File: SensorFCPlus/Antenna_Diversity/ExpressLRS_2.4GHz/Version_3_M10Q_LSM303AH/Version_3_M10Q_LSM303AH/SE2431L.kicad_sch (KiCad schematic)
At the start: 8 parts, among them U7 SE2431L-R

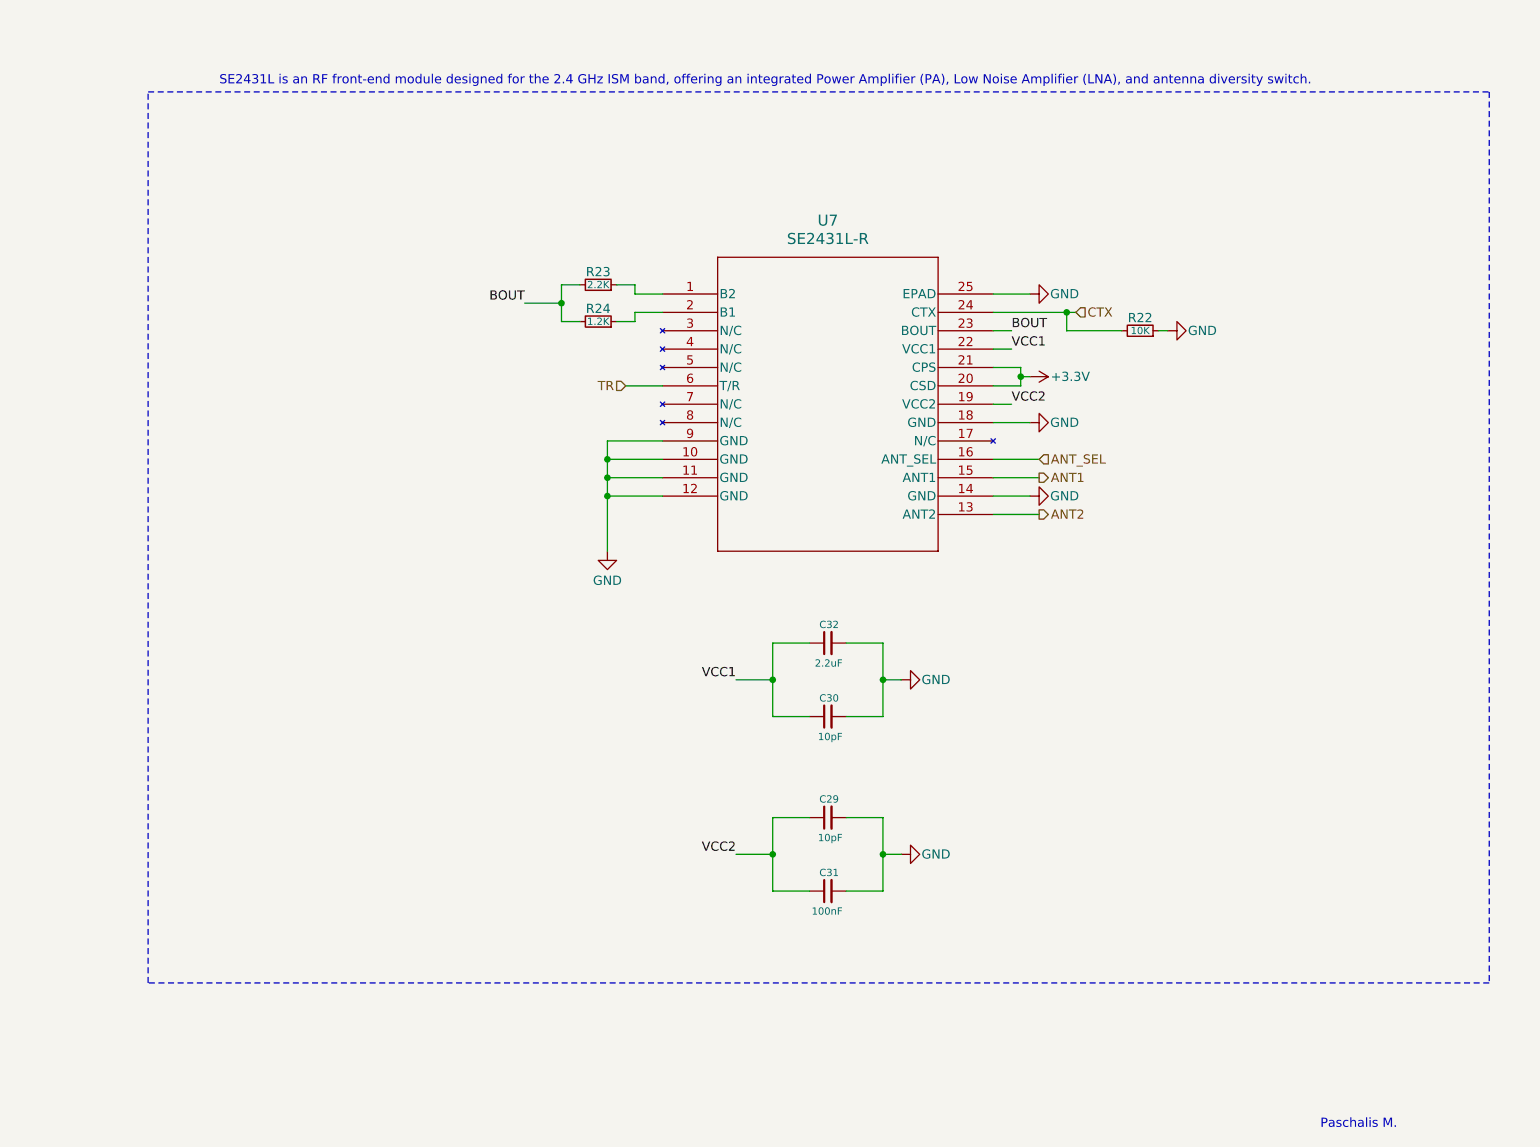
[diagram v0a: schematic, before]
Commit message: Update PCB design for Version 3 M10Q LSM303AH (ESP8285, SE2431L, SX1280, and main board)
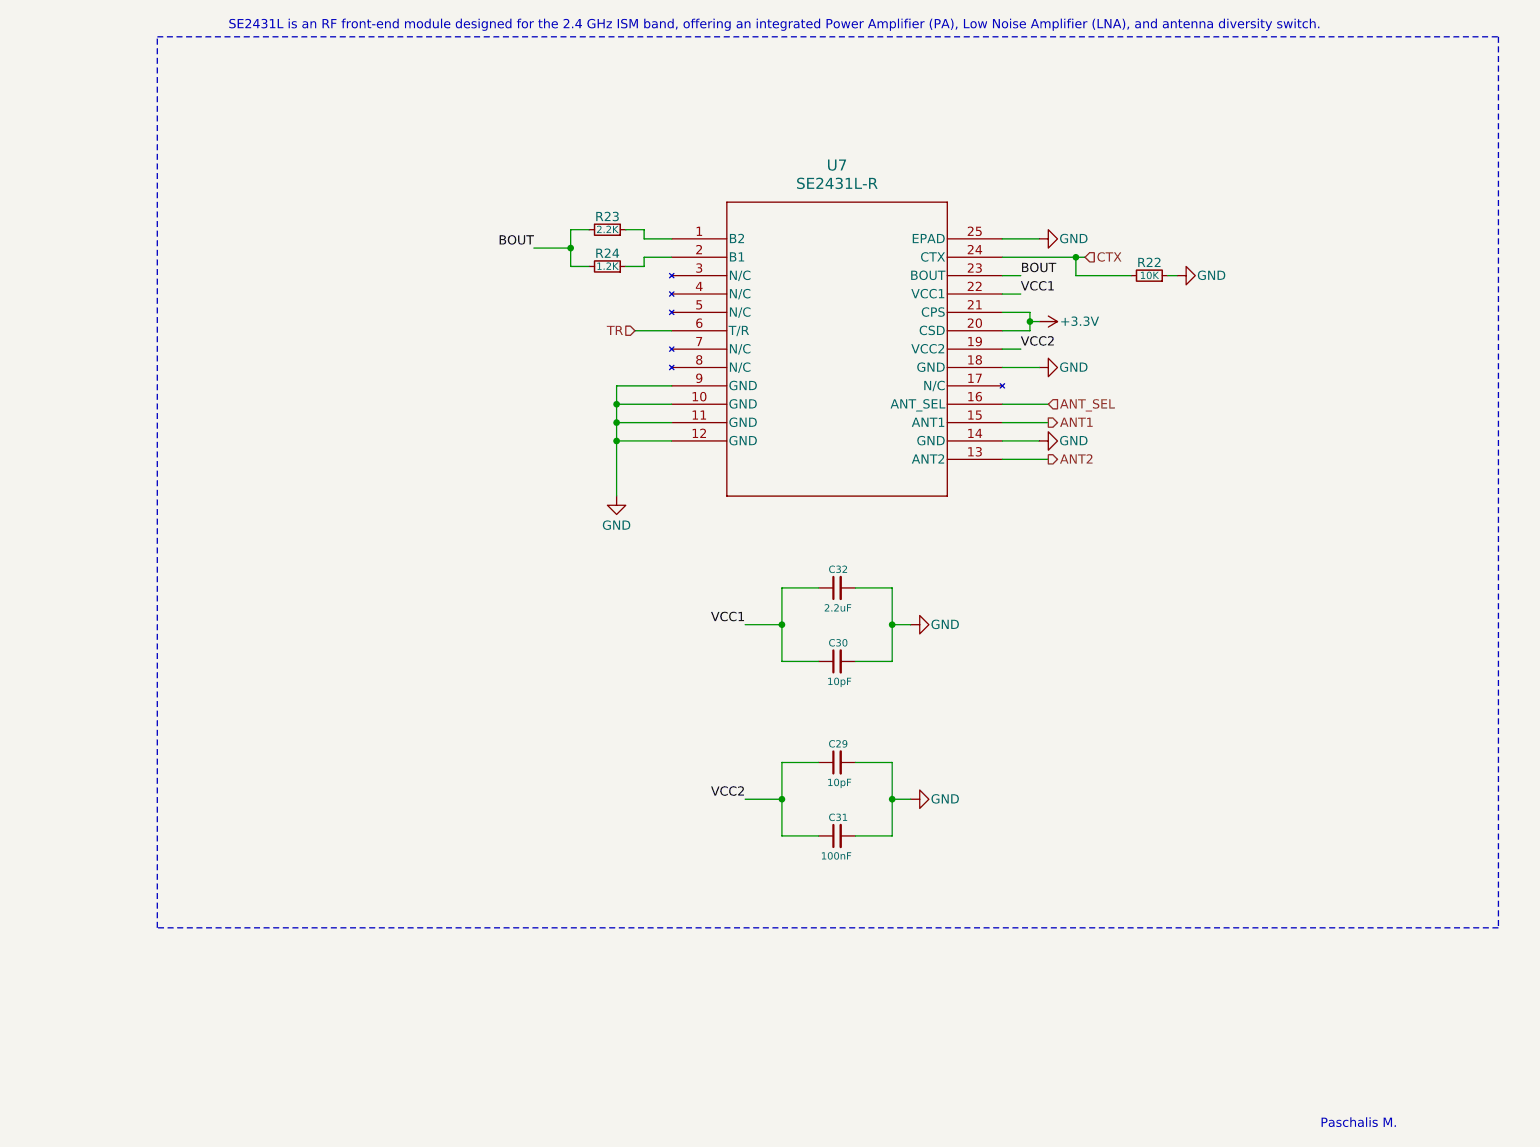
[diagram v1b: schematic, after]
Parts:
- C29, C30, C31, C32: footprint Capacitor_SMD:C_0805_2012Metric_Pad1.18x1.45mm_HandSolder -> Capacitor_SMD:C_0603_1608Metric_Pad1.08x0.95mm_HandSolder
- R22, R23, R24: footprint Resistor_SMD:R_0805_2012Metric_Pad1.20x1.40mm_HandSolder -> Resistor_SMD:R_0603_1608Metric_Pad0.98x0.95mm_HandSolder
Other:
- moved on the sheet: C29, C30, C31, C32, R22, R23, R24, U7

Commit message: Updated Version_3_M10Q_LSM303AH
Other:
- title: (none) -> SE2431L
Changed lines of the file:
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@@
 	(paper "A4")
 	(title_block
+		(title "SE2431L")
 		(date "05-01-2025")
 		(rev "1.0")
@@
 	(label "BOUT"
 		(at 100.33 62.23 180)
-		(fields_autoplaced yes)
 		(effects
 			(font
@@
 	(label "BOUT"
 		(at 167.64 66.04 0)
-		(fields_autoplaced yes)
 		(effects
 			(font
@@
 	(label "VCC2"
 		(at 129.54 138.43 180)
-		(fields_autoplaced yes)
 		(effects
 			(font
@@
 	(label "VCC1"
 		(at 167.64 68.58 0)
-		(fields_autoplaced yes)
 		(effects
 			(font
@@
 	(label "VCC2"
 		(at 167.64 76.2 0)
-		(fields_autoplaced yes)
 		(effects
 			(font
@@
 	(label "VCC1"
 		(at 129.54 114.3 180)
-		(fields_autoplaced yes)
 		(effects
 			(font
@@
 		(shape input)
 		(at 176.53 63.5 0)
-		(fields_autoplaced yes)
 		(effects
 			(font
@@
 		(shape input)
 		(at 114.3 73.66 180)
-		(fields_autoplaced yes)
 		(effects
 			(font
@@
 		(shape output)
 		(at 171.45 86.36 0)
-		(fields_autoplaced yes)
 		(effects
 			(font
@@
 		(shape input)
 		(at 171.45 83.82 0)
-		(fields_autoplaced yes)
 		(effects
 			(font
@@
 		(shape output)
 		(at 171.45 91.44 0)
-		(fields_autoplaced yes)
-		(effects
-			(font
+		(effects
+			(font
